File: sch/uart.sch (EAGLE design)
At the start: 10 parts

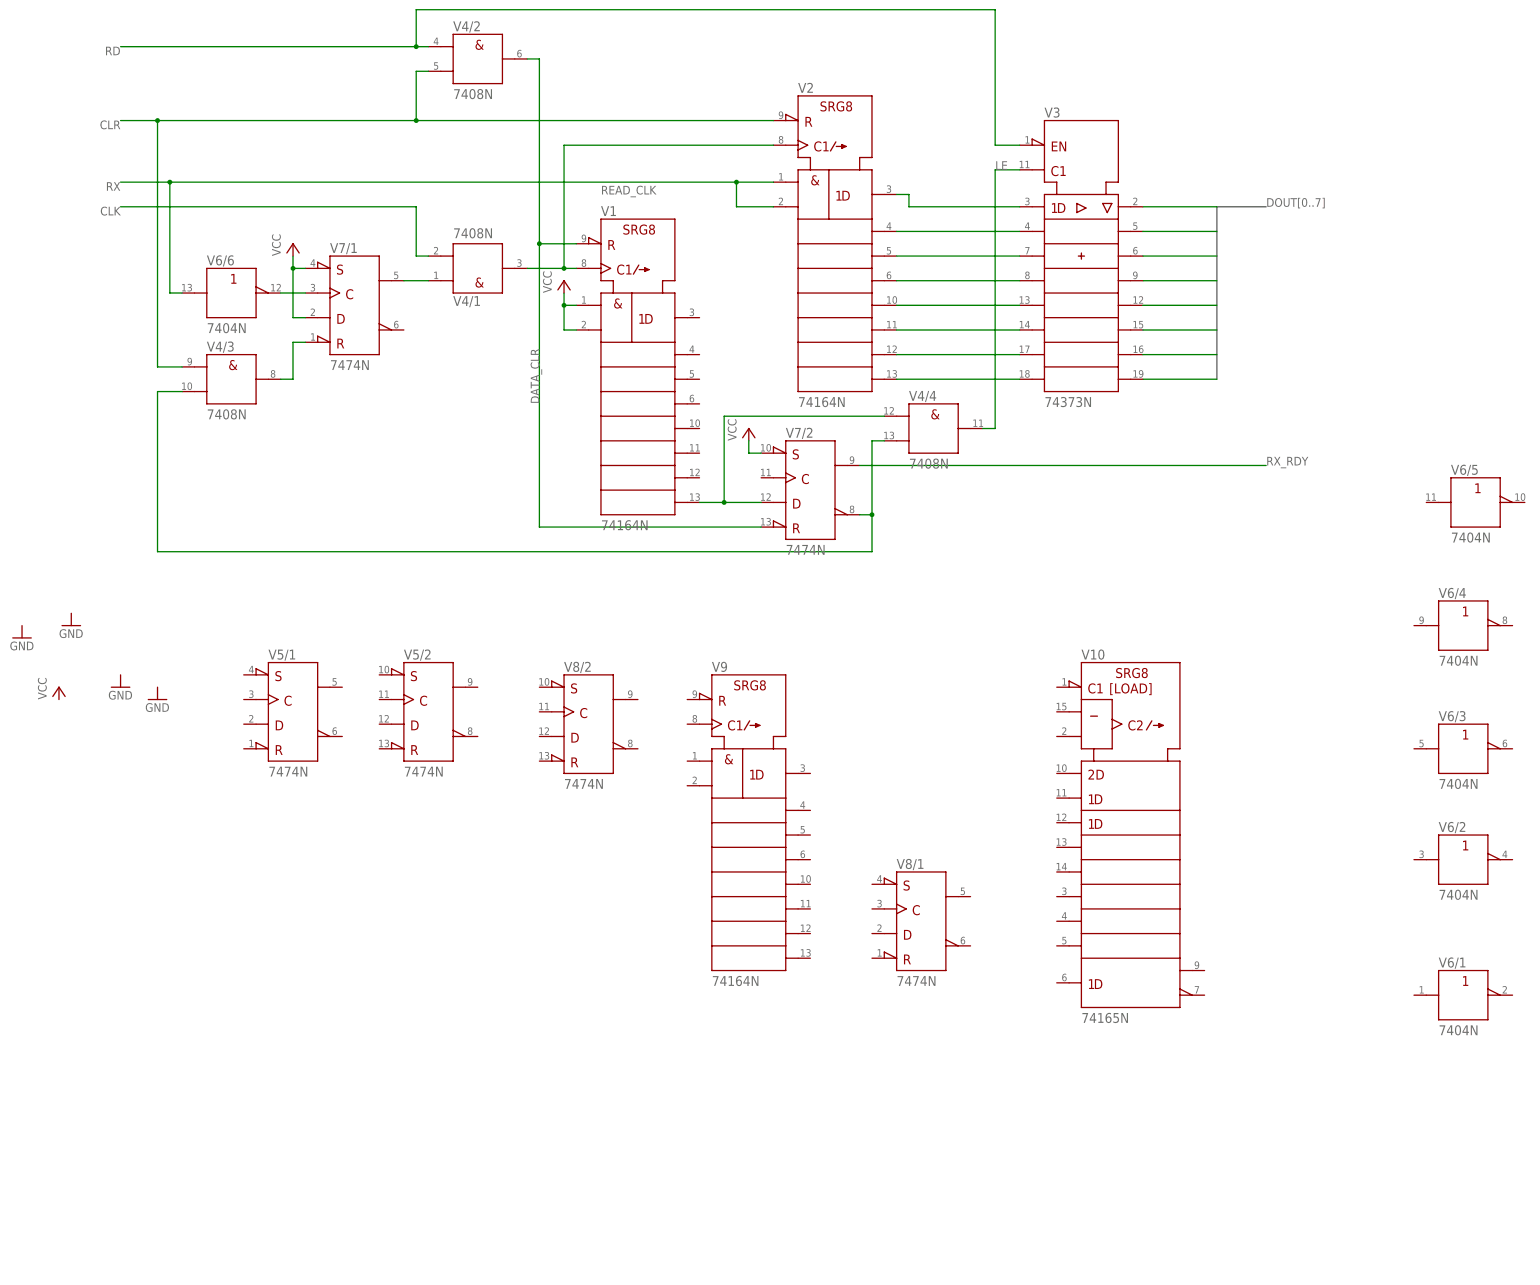
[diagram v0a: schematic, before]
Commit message: Added transmitter circuit schematic.
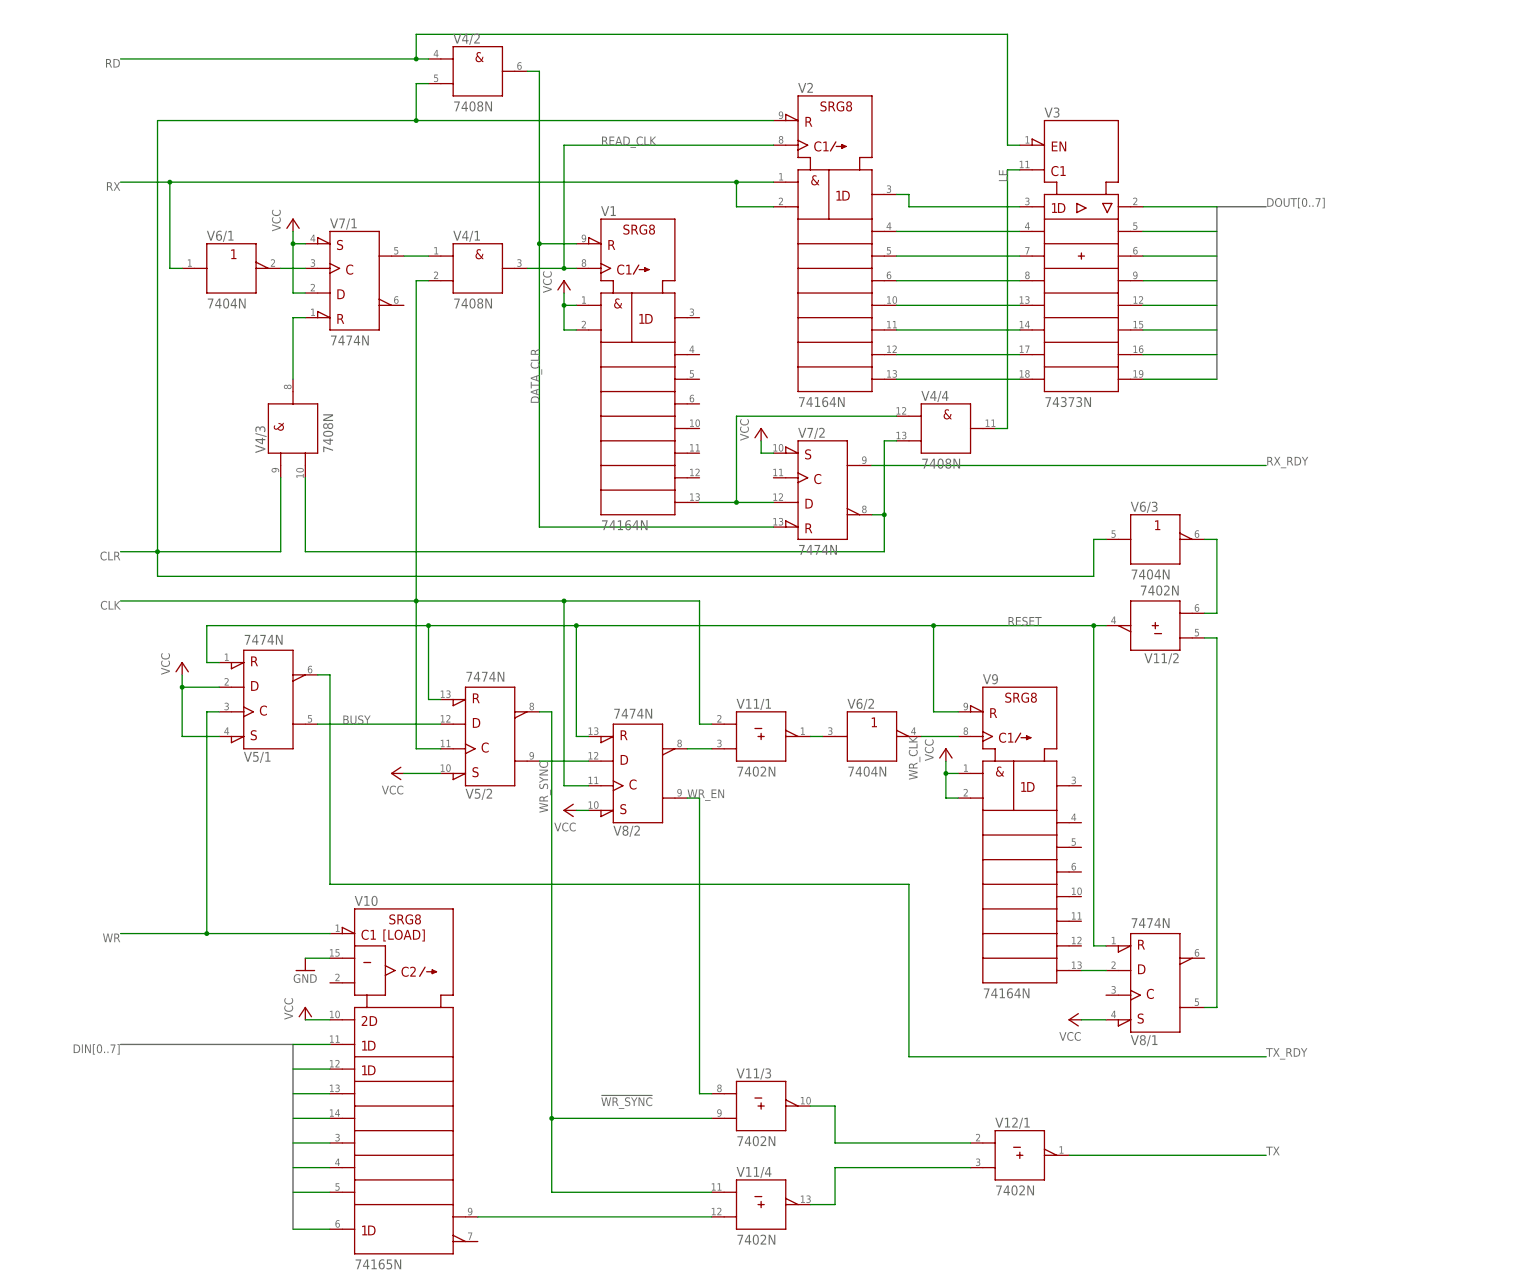
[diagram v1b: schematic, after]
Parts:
- added V11, V12: 7402N, 74ttl-din:7402N
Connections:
- new net !TX_DATA_FIXED!: V11/4.Y, V12/1.B
- new net !WR_EN!: V11/1.B, V8/2.!Q
- new net !WR_SYNC!: V11/3.B, V11/4.A, V5/2.!Q
- new net BUSY: V5/1.Q, V5/2.D
- new net DIN0: V101.H
- new net DIN1: V101.G
- new net DIN2: V101.F
- new net DIN3: V101.E
- new net DIN4: V101.D
- new net DIN5: V101.C
- new net DIN6: V101.B
- new net DIN7: V101.A
- new net DONE: V11/2.A, V8/1.Q
- new net GND: V101.CLK_INH
- new net N$13: V8/1.D, V91.QH
- new net N$14: V11/1.Y, V6/2.A
- new net N$15: V11/2.B, V6/3.Y
- new net RESET: V11/2.Y, V5/1.!CLR, V5/2.!CLR, V8/1.!CLR, V8/2.!CLR, V91.!CLR
- new net START_BIT: V11/3.Y, V12/1.A
- new net TX: V12/1.Y
- new net TX_DATA: V101.QH, V11/4.B
- new net TX_RDY: V5/1.!Q
- new net WR: V101.SH/!LD, V5/1.CLK
- new net WR_CLK: V6/2.Y, V91.CLK
- new net WR_EN: V11/3.A, V8/2.Q
- new net WR_SYNC: V5/2.Q, V8/2.D
- net CLK: now also V11/1.A, V5/2.CLK, V8/2.CLK
- net CLR: now also V6/3.A
- net N$12: now also V6/1.Y; no longer V6/6.Y
- net RX: now also V6/1.A; no longer V6/6.A
- net VCC: now also V101.SER, V5/1.!PRE, V5/1.D, V5/2.!PRE, V8/1.!PRE, V8/2.!PRE, V91.A, V91.B
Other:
- moved on the sheet: V10, V4/1, V4/2, V4/3, V4/4, V5/1, V5/2, V6/1, V6/2, V6/3, V7/1, V7/2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

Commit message: Replaced 74XX04 with leftover 74X02's.
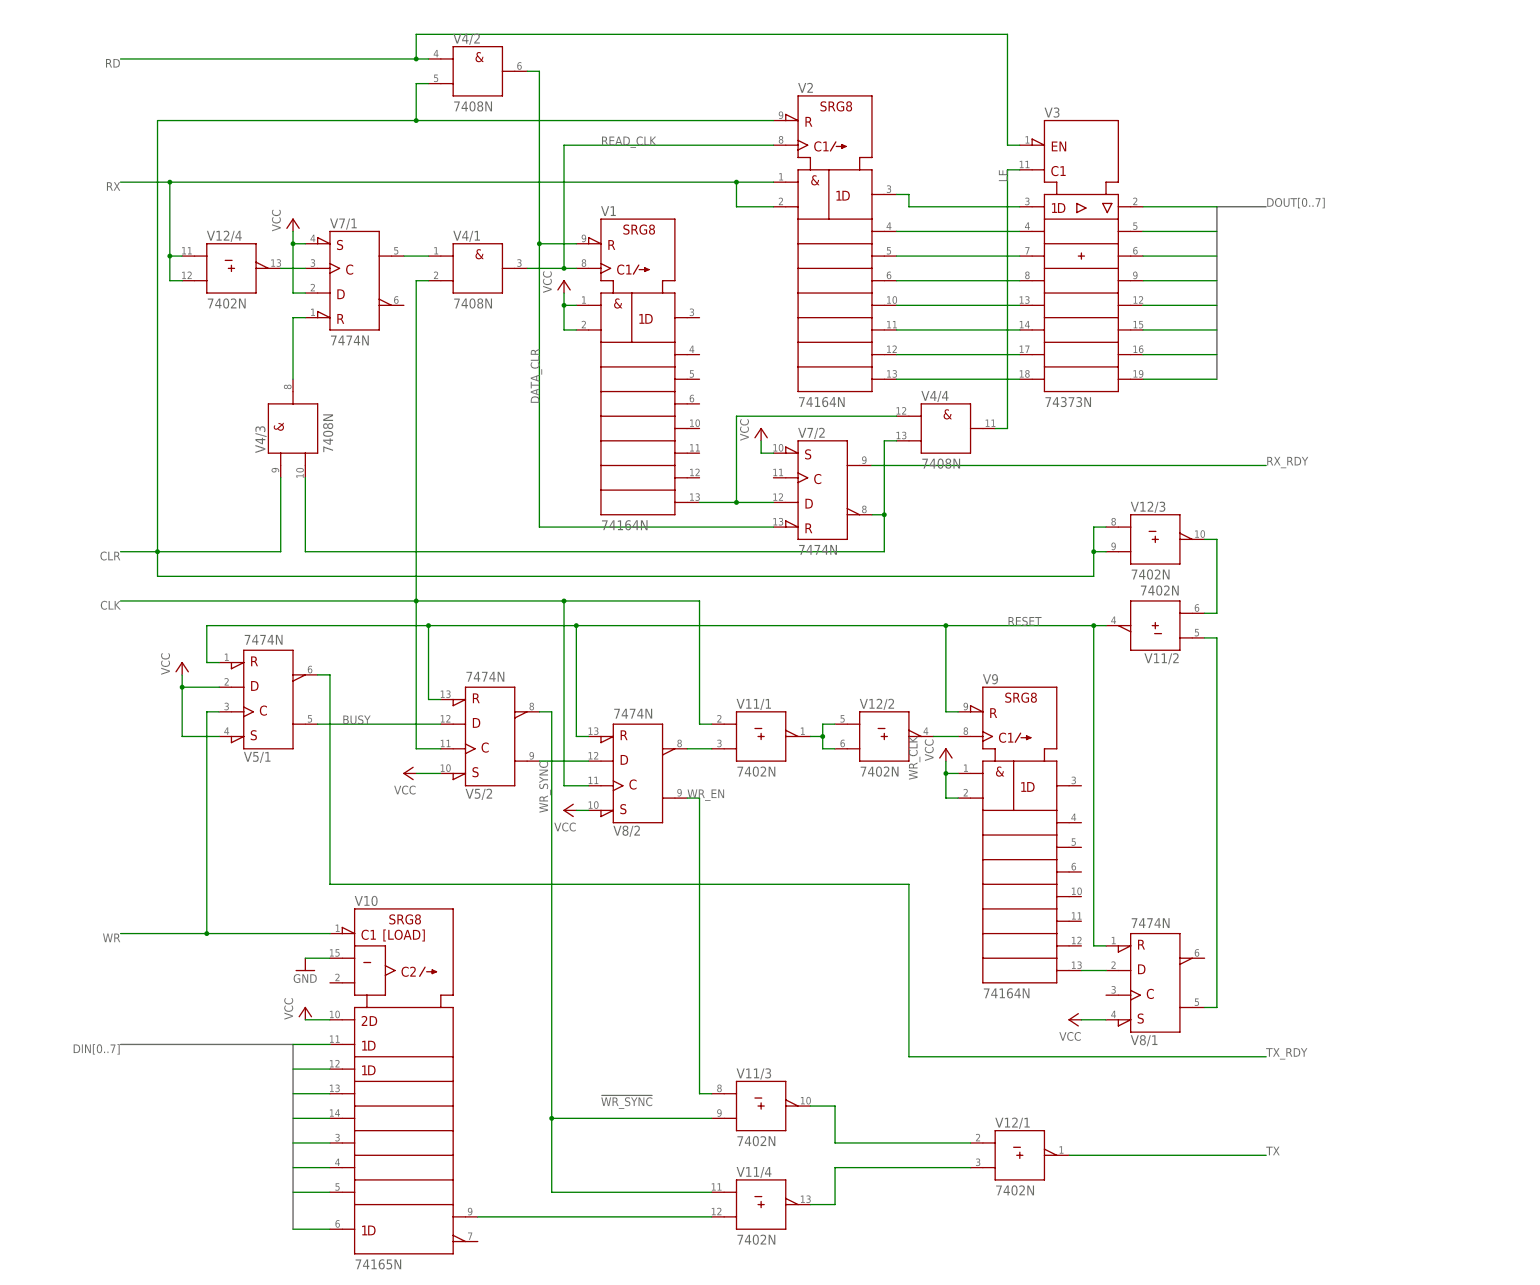
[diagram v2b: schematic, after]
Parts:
- removed V6: 7404N, 74ttl-din:7404N
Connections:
- net CLR: now also V12/3.A, V12/3.B; no longer V6/3.A
- net N$12: now also V12/4.Y; no longer V6/1.Y
- net N$14: now also V12/2.A, V12/2.B; no longer V6/2.A
- net N$15: now also V12/3.Y; no longer V6/3.Y
- net RX: now also V12/4.A, V12/4.B; no longer V6/1.A
- net WR_CLK: now also V12/2.Y; no longer V6/2.Y
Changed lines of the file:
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@@
 <part name="V3" library="74ttl-din" deviceset="74*373" device="N"/>
 <part name="V4" library="74ttl-din" deviceset="74*08" device="N"/>
-<part name="V6" library="74ttl-din" deviceset="74*04" device="N"/>
 <part name="V7" library="74ttl-din" deviceset="74*74" device="N"/>
 <part name="V5" library="74ttl-din" deviceset="74*74" device="N"/>
@@
 <instance part="V4" gate="/3" x="17.78" y="101.6" rot="R90"/>
 <instance part="V4" gate="/4" x="152.4" y="101.6"/>
-<instance part="V6" gate="/1" x="5.08" y="134.62"/>
-<instance part="V6" gate="/2" x="137.16" y="38.1"/>
-<instance part="V6" gate="/3" x="195.58" y="78.74"/>
 <instance part="V7" gate="/1" x="30.48" y="132.08"/>
 <instance part="V7" gate="/2" x="127" y="88.9"/>
@@
 <instance part="P+3" gate="VCC" x="114.3" y="101.6"/>
 <instance part="P+4" gate="VCC" x="-5.08" y="53.34"/>
-<instance part="P+5" gate="VCC" x="38.1" y="30.48" rot="R90"/>
+<instance part="P+5" gate="VCC" x="40.64" y="30.48" rot="R90"/>
 <instance part="P+6" gate="VCC" x="73.66" y="22.86" rot="R90"/>
 <instance part="V11" gate="/1" x="114.3" y="38.1"/>
@@
 <instance part="P+9" gate="VCC" x="20.32" y="-17.78"/>
 <instance part="V12" gate="/1" x="167.64" y="-48.26"/>
+<instance part="V12" gate="/2" x="139.7" y="38.1"/>
+<instance part="V12" gate="/3" x="195.58" y="78.74"/>
+<instance part="V12" gate="/4" x="5.08" y="134.62"/>
 </instances>
 <busses>
@@
 <wire x1="116.84" y1="152.4" x2="109.22" y2="152.4" width="0.1524" layer="91"/>
 <junction x="109.22" y="152.4"/>
-<wire x1="-5.08" y1="134.62" x2="-7.62" y2="134.62" width="0.1524" layer="91"/>
-<wire x1="-7.62" y1="134.62" x2="-7.62" y2="152.4" width="0.1524" layer="91"/>
+<wire x1="-5.08" y1="132.08" x2="-7.62" y2="132.08" width="0.1524" layer="91"/>
+<wire x1="-7.62" y1="132.08" x2="-7.62" y2="137.16" width="0.1524" layer="91"/>
 <junction x="-7.62" y="152.4"/>
-<pinref part="V6" gate="/1" pin="A"/>
+<pinref part="V12" gate="/4" pin="B"/>
+<pinref part="V12" gate="/4" pin="A"/>
+<wire x1="-7.62" y1="137.16" x2="-7.62" y2="152.4" width="0.1524" layer="91"/>
+<wire x1="-5.08" y1="137.16" x2="-7.62" y2="137.16" width="0.1524" layer="91"/>
+<junction x="-7.62" y="137.16"/>
 </segment>
 </net>
@@
 <pinref part="V5" gate="/2" pin="!PRE"/>
 <pinref part="P+5" gate="VCC" pin="VCC"/>
-<wire x1="48.26" y1="30.48" x2="40.64" y2="30.48" width="0.1524" layer="91"/>
+<wire x1="48.26" y1="30.48" x2="43.18" y2="30.48" width="0.1524" layer="91"/>
 </segment>
 <segment>
@@
 <wire x1="-10.16" y1="76.2" x2="-10.16" y2="71.12" width="0.1524" layer="91"/>
 <wire x1="-10.16" y1="71.12" x2="182.88" y2="71.12" width="0.1524" layer="91"/>
-<wire x1="182.88" y1="71.12" x2="182.88" y2="78.74" width="0.1524" layer="91"/>
-<pinref part="V6" gate="/3" pin="A"/>
-<wire x1="182.88" y1="78.74" x2="185.42" y2="78.74" width="0.1524" layer="91"/>
+<wire x1="182.88" y1="71.12" x2="182.88" y2="76.2" width="0.1524" layer="91"/>
+<wire x1="182.88" y1="76.2" x2="182.88" y2="81.28" width="0.1524" layer="91"/>
+<wire x1="182.88" y1="81.28" x2="185.42" y2="81.28" width="0.1524" layer="91"/>
+<pinref part="V12" gate="/3" pin="A"/>
+<pinref part="V12" gate="/3" pin="B"/>
+<wire x1="185.42" y1="76.2" x2="182.88" y2="76.2" width="0.1524" layer="91"/>
+<junction x="182.88" y="76.2"/>
 </segment>
 </net>
@@
 <pinref part="V7" gate="/1" pin="CLK"/>
 <wire x1="20.32" y1="134.62" x2="15.24" y2="134.62" width="0.1524" layer="91"/>
-<pinref part="V6" gate="/1" pin="Y"/>
+<pinref part="V12" gate="/4" pin="Y"/>
 </segment>
 </net>
@@
 <label x="165.1" y="60.96" size="1.778" layer="95"/>
 <pinref part="V9" gate="1" pin="!CLR"/>
-<wire x1="154.94" y1="43.18" x2="149.86" y2="43.18" width="0.1524" layer="91"/>
-<wire x1="149.86" y1="43.18" x2="149.86" y2="60.96" width="0.1524" layer="91"/>
-<wire x1="149.86" y1="60.96" x2="76.2" y2="60.96" width="0.1524" layer="91"/>
+<wire x1="154.94" y1="43.18" x2="152.4" y2="43.18" width="0.1524" layer="91"/>
+<wire x1="152.4" y1="43.18" x2="152.4" y2="60.96" width="0.1524" layer="91"/>
+<wire x1="152.4" y1="60.96" x2="76.2" y2="60.96" width="0.1524" layer="91"/>
 <junction x="76.2" y="60.96"/>
 <wire x1="0" y1="60.96" x2="0" y2="53.34" width="0.1524" layer="91"/>
 <wire x1="0" y1="53.34" x2="2.54" y2="53.34" width="0.1524" layer="91"/>
-<wire x1="149.86" y1="60.96" x2="182.88" y2="60.96" width="0.1524" layer="91"/>
+<wire x1="152.4" y1="60.96" x2="182.88" y2="60.96" width="0.1524" layer="91"/>
 <pinref part="V8" gate="/1" pin="!CLR"/>
 <wire x1="182.88" y1="60.96" x2="182.88" y2="-5.08" width="0.1524" layer="91"/>
 <wire x1="182.88" y1="-5.08" x2="185.42" y2="-5.08" width="0.1524" layer="91"/>
-<junction x="149.86" y="60.96"/>
+<junction x="152.4" y="60.96"/>
 <pinref part="V11" gate="/2" pin="Y"/>
 <wire x1="185.42" y1="60.96" x2="182.88" y2="60.96" width="0.1524" layer="91"/>
@@
 <net name="WR_CLK" class="0">
 <segment>
-<pinref part="V6" gate="/2" pin="Y"/>
 <pinref part="V9" gate="1" pin="CLK"/>
-<wire x1="147.32" y1="38.1" x2="154.94" y2="38.1" width="0.1524" layer="91"/>
+<wire x1="149.86" y1="38.1" x2="154.94" y2="38.1" width="0.1524" layer="91"/>
 <label x="144.78" y="38.1" size="1.778" layer="95" rot="R270"/>
+<pinref part="V12" gate="/2" pin="Y"/>
 </segment>
 </net>
@@
 <net name="N$14" class="0">
 <segment>
-<pinref part="V6" gate="/2" pin="A"/>
 <pinref part="V11" gate="/1" pin="Y"/>
 <wire x1="127" y1="38.1" x2="124.46" y2="38.1" width="0.1524" layer="91"/>
+<pinref part="V12" gate="/2" pin="A"/>
+<wire x1="129.54" y1="40.64" x2="127" y2="40.64" width="0.1524" layer="91"/>
+<wire x1="127" y1="40.64" x2="127" y2="38.1" width="0.1524" layer="91"/>
+<pinref part="V12" gate="/2" pin="B"/>
+<wire x1="129.54" y1="35.56" x2="127" y2="35.56" width="0.1524" layer="91"/>
+<wire x1="127" y1="35.56" x2="127" y2="38.1" width="0.1524" layer="91"/>
+<junction x="127" y="38.1"/>
 </segment>
 </net>
@@
 <wire x1="205.74" y1="63.5" x2="208.28" y2="63.5" width="0.1524" layer="91"/>
 <wire x1="208.28" y1="63.5" x2="208.28" y2="78.74" width="0.1524" layer="91"/>
-<pinref part="V6" gate="/3" pin="Y"/>
 <wire x1="208.28" y1="78.74" x2="205.74" y2="78.74" width="0.1524" layer="91"/>
-</segment>
-</net>
+<pinref part="V12" gate="/3" pin="Y"/>
+</segment>
+</net>
